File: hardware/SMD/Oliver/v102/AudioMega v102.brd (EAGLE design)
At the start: 77.1 x 44.9 mm, 74 parts, among them Q1 BC846ASMD, Q2 BC846ASMD, Q3 BC846ASMD, Q4 2N7002, Q5 BC846ASMD, U1 REG1117-5, U2 REG1117-3.3, U3 ATMEGA328-AU, U4 LM386M, X1 12MHz

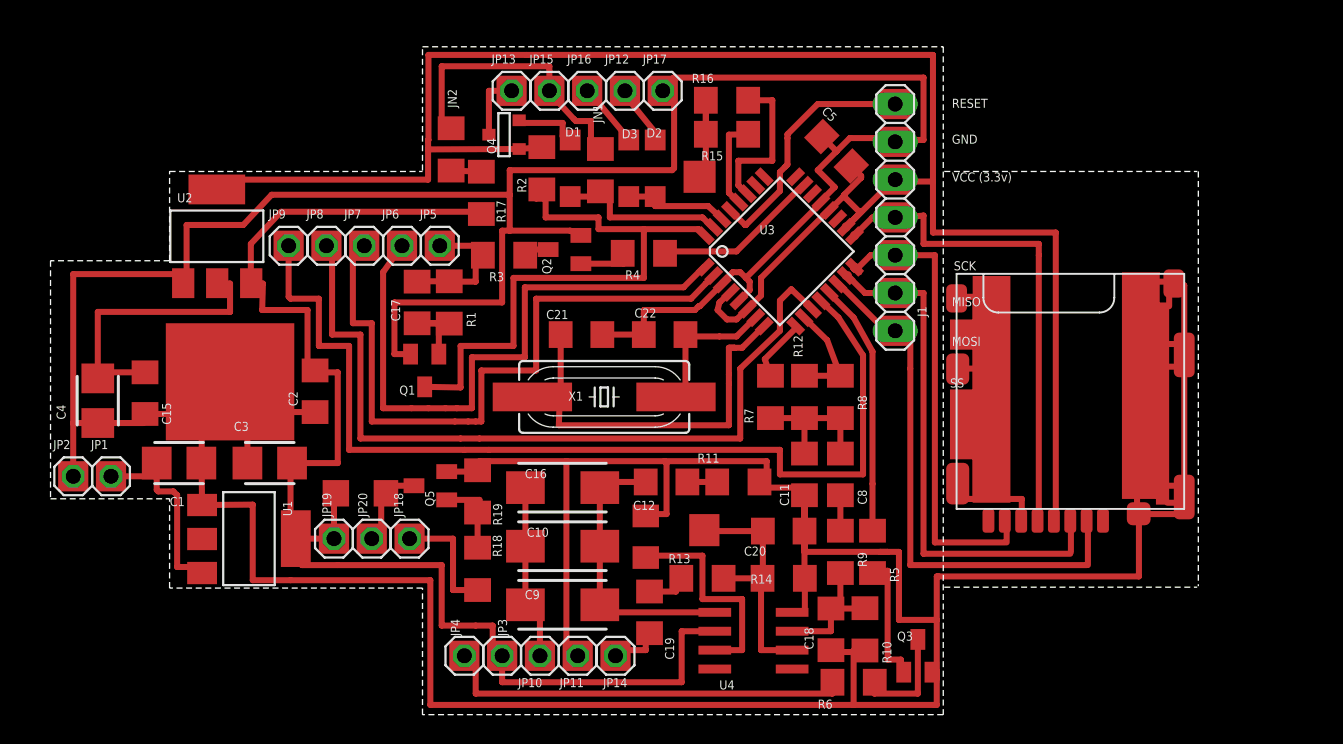
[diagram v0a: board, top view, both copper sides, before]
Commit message: updated v102 board + added connector for haptic motor + added last schematic changes from MikeB (connection to M64) + added last audio filter changes (filtering PWM noise) from Mike and Hans
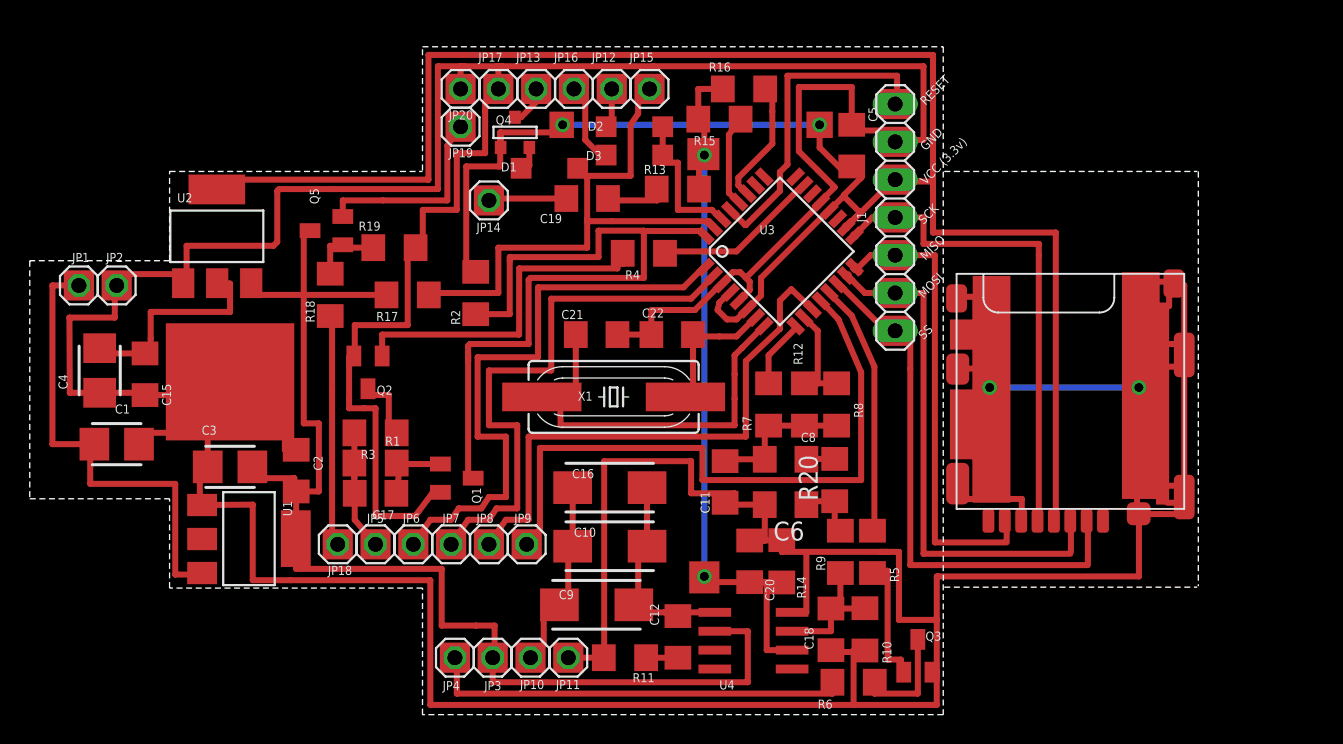
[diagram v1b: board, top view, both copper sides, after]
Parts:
- removed JN1, JN2: 0, resistor:R1206
- added C6: 330pf, resistor:C1206
- added R20: 47k, resistor:R1206
- R9: value 33k -> 47k
- moved JP14 31.8 mm to (29.5, 51.1)
- moved JP20 30.8 mm to (27.6, 58.5)
- moved JP19 29.0 mm to (27.6, 56.0)
- moved C19 28.1 mm to (36.1, 51.2), turned to 0 degrees
- moved R13 26.2 mm to (42.2, 51.8)
- moved JP9 25.7 mm to (32.0, 27.9)
- moved JP8 22.8 mm to (29.5, 27.9)
- moved R18 20.9 mm to (18.8, 44.7)
- moved JP7 20.9 mm to (26.9, 27.9)
- moved JP5 20.5 mm to (21.8, 27.9)
- moved JP6 20.1 mm to (24.4, 27.9)
- moved Q5 18.5 mm to (18.5, 49.0)
- moved R19 17.3 mm to (23.1, 47.9), turned to 0 degrees
- moved Q2 15.6 mm to (21.3, 39.5), turned to 180 degrees
- moved R3 14.7 mm to (21.8, 35.4)
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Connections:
- removed net N$14: U4.7
- removed net N$22: JN2.1, R17.1
- removed net N$44: JP20.1, Q5.3
- new net N$61: C8.1, R20.2
- net +5V: now also Q5.3; no longer JP19.1
- net GND: now also C6.2, JP20.1; no longer Q5.2
- net N$2: now also JP19.1, Q5.2; no longer JN1.2, JN2.2, JP15.1
- net N$24: now also C6.1, R20.1; no longer C8.1
- net N$38: now also JP15.1, R17.1; no longer JN1.1
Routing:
- net N$38: track 11.3 -> 41.1 mm
- net VOL_B: track 25.1 -> 54.2 mm, vias 0 -> 2
- net N$58: track 151.6 -> 178.3 mm, vias 0 -> 2
- net GND: track 362.3 -> 388.8 mm
- net N$30: track 66.6 -> 43.4 mm
- net N$9: track 3.58 -> 23.1 mm
- net N$32: track 14.8 -> 31.9 mm
- net N$31: track 53.9 -> 36.9 mm
- net CLK: track 39.7 -> 50.3 mm
- net N$40: track 8.03 -> 16.4 mm
- net N$35: track 45.3 -> 37.5 mm
- net N$44: track 6.94 -> 0.00 mm
- net +5V: track 93.6 -> 87.0 mm
- net N$2: track 19.6 -> 13.3 mm
- net N$6: track 17.5 -> 22.8 mm
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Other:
- board size 77.1 x 44.9 mm -> 78.5 x 44.9 mm

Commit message: updated v102 board - corrected BAT & GND pads
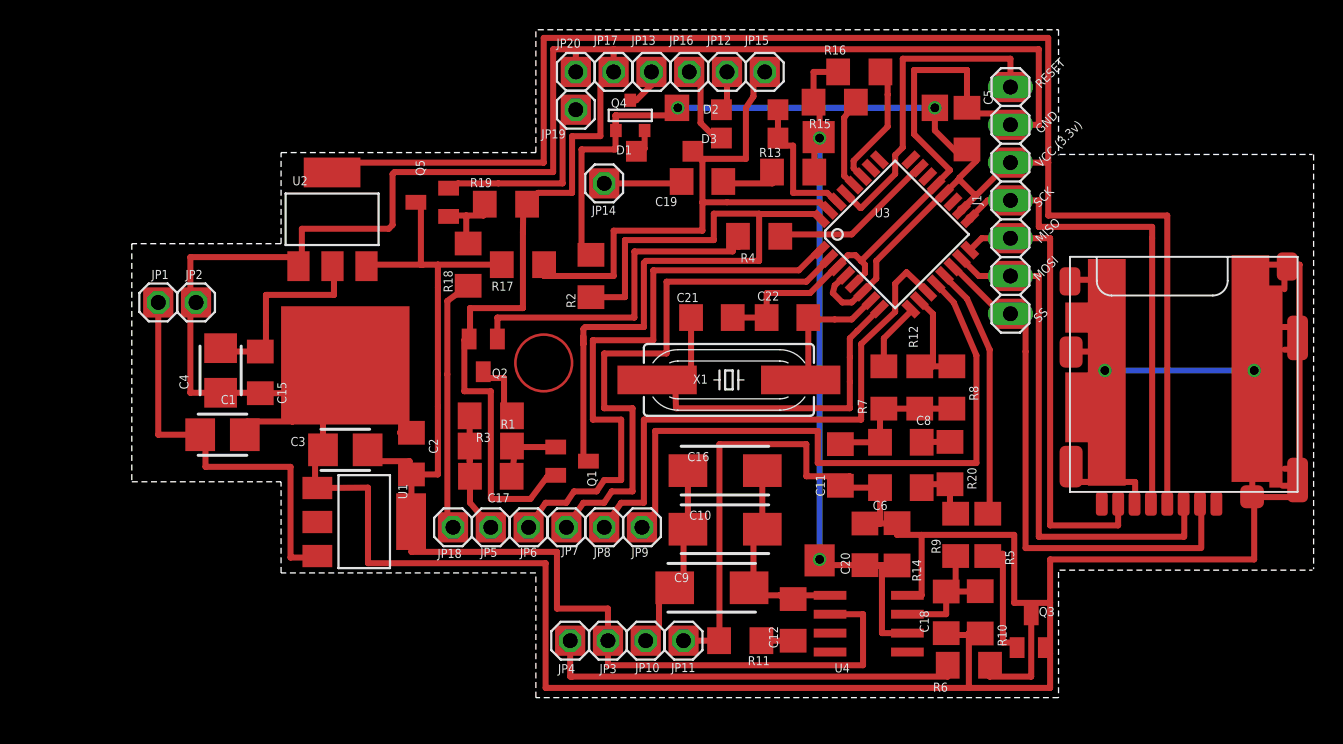
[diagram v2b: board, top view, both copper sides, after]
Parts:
- moved R18 9.49 mm to (28.1, 46.7)
- moved C4 8.13 mm to (11.4, 39.6)
- moved R19 8.04 mm to (30.6, 50.8)
- moved R17 8.01 mm to (31.8, 46.7)
- moved J1 7.83 mm to (64.5, 51.1)
- moved X1 7.83 mm to (45.6, 39.0)
- moved JP3 7.83 mm to (37.5, 21.5)
- moved R2 7.83 mm to (36.3, 46.0)
- moved C3 7.83 mm to (19.8, 34.3)
- moved C10 7.83 mm to (45.3, 29.0)
- moved C11 7.83 mm to (53.1, 33.3)
- moved C12 7.83 mm to (49.9, 22.9)
- moved C16 7.83 mm to (45.3, 32.9)
- moved C17 7.83 mm to (29.6, 32.5)
- moved C18 7.83 mm to (60.2, 23.4)
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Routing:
- net GND: track 388.8 -> 375.6 mm
- net N$32: track 31.9 -> 28.7 mm
- net N$46: track 0.76 -> 2.29 mm
- net N$58: track 178.3 -> 177.1 mm
- net N$6: track 22.8 -> 21.8 mm
- net N$4: track 30.5 -> 29.6 mm
- net VOL_B: track 54.2 -> 53.4 mm
- net N$40: track 16.4 -> 17.1 mm
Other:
- board size 78.5 x 44.9 mm -> 79.4 x 44.9 mm

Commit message: updated v102 board - checked for Gerber export - add Gerber files
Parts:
- moved C2 12.7 mm to (24.1, 46.7), turned to 270 degrees
- moved R15 0.25 mm to (52.7, 57.4)
- moved C1 0.13 mm to (11.6, 35.4)
- moved R20 0.13 mm to (60.6, 33.4)
- moved R19 0.13 mm to (30.6, 50.7)
- renumbered JP1 to UB+, JP10 to SP+, JP11 to SP-, JP12 to PD2, JP13 to TX, JP14 to BEP, JP15 to PD3, JP16 to RX, JP17 to GND, JP18 to PG2, JP19 to HAP+, JP2 to UGND, JP20 to HAPG, JP3 to BL+, JP4 to BL-, JP5 to PB7, JP6 to LCD0, JP7 to LCD1, JP8 to LCD2, JP9 to LCD3
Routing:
- net GND: track 375.6 -> 386.2 mm
- net +5V: track 87.1 -> 88.2 mm
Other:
- board text added: "(3.3v)"
- board text added: "RES"
- board text added: "TTL 5v uart"
- board text added: "VCC"
- board text added: "m64"
- board text removed: "RESET"
- board text removed: "VCC (3.3v)"

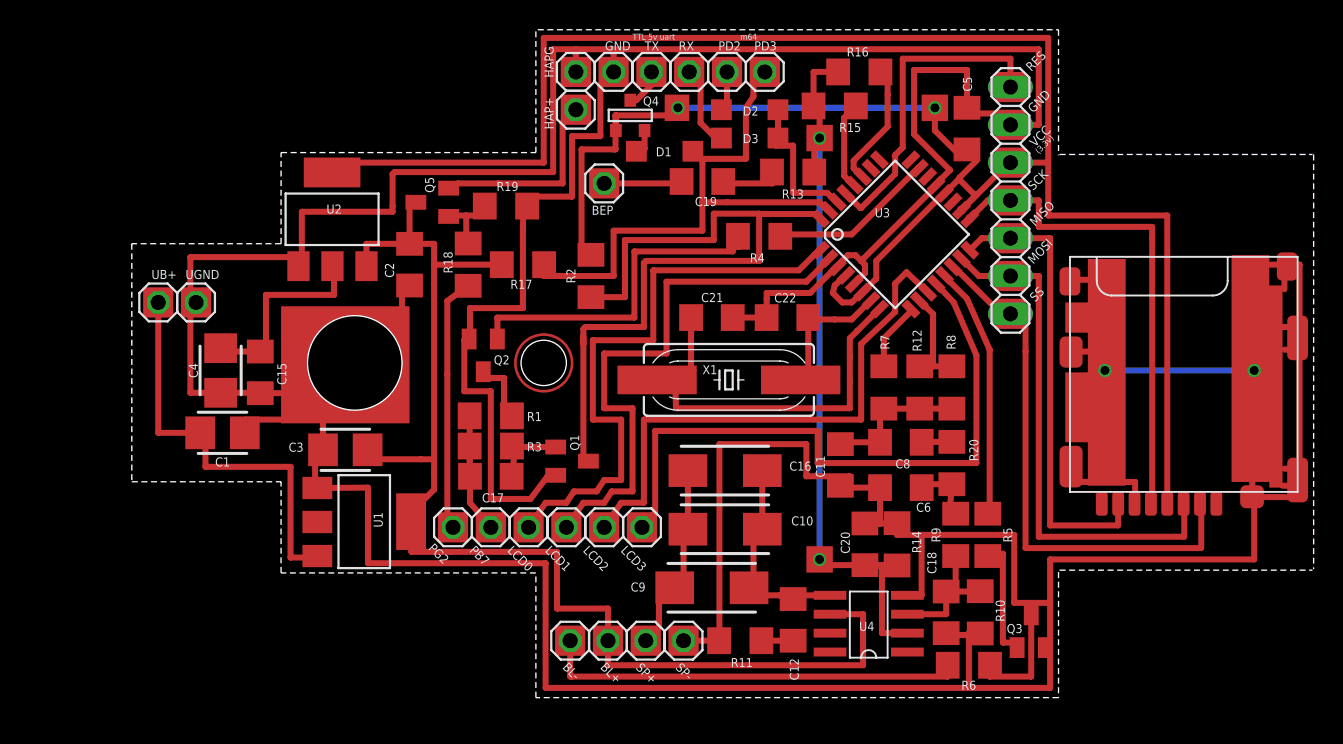
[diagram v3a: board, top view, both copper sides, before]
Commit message: updated v102 board - some minore changes for home etching
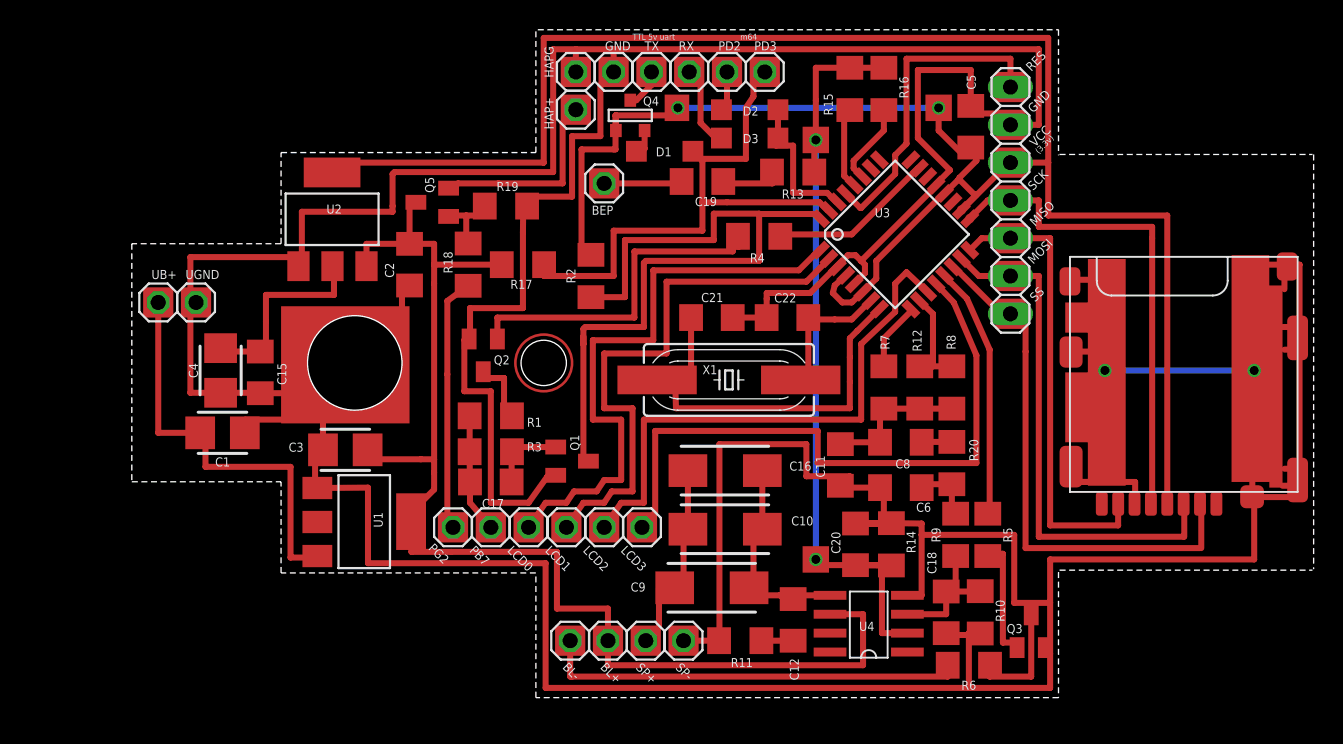
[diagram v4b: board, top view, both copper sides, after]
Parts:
- moved R16 2.01 mm to (56.0, 58.5), turned to 90 degrees
- moved R15 1.53 mm to (53.7, 58.5), turned to 90 degrees
- moved C20 0.64 mm to (54.1, 27.9)
- moved C17 0.38 mm to (29.6, 32.1)
- moved R1 0.38 mm to (29.6, 34.2)
- moved R14 0.38 mm to (56.5, 27.9)
- moved C5 0.28 mm to (61.8, 56.0)
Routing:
- net N$10: track 9.26 -> 5.59 mm
- net GND: track 386.2 -> 389.0 mm
- net VOL_B: track 53.8 -> 55.6 mm
- net N$13: track 6.18 -> 5.31 mm

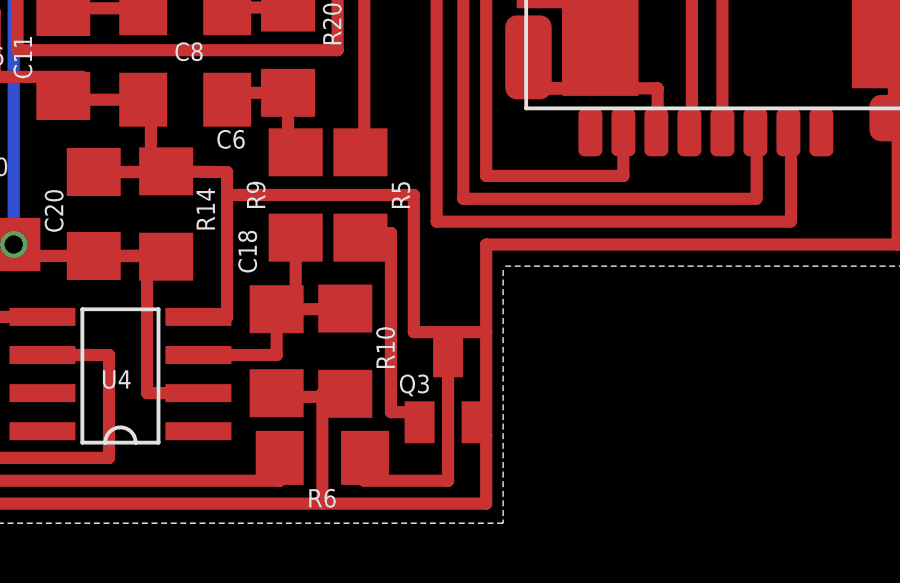
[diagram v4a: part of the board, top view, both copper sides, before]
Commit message: - fixed error near Q3
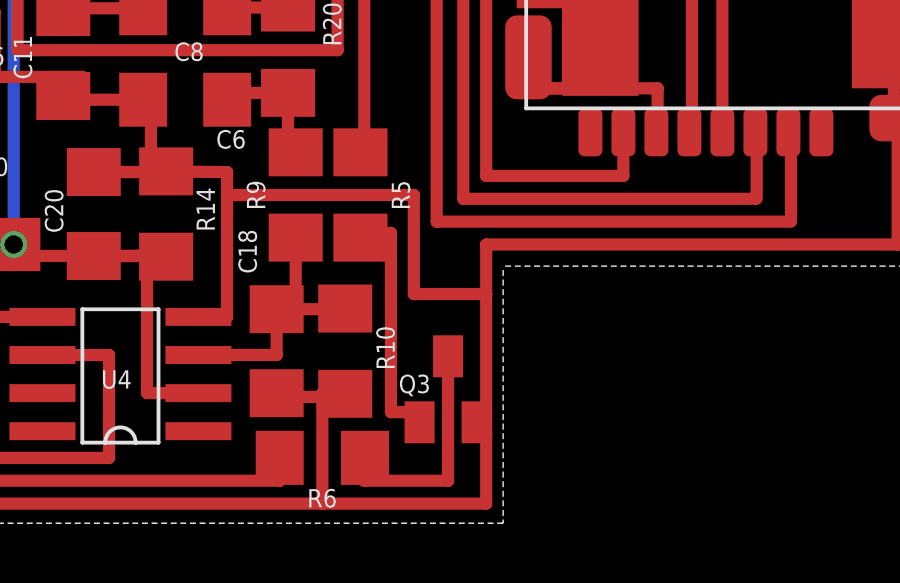
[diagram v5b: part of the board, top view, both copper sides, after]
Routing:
- net GND: track 389.0 -> 387.8 mm
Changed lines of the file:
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@@
 <layer number="17" name="Pads" color="2" fill="1" visible="yes" active="yes"/>
 <layer number="18" name="Vias" color="2" fill="1" visible="yes" active="yes"/>
-<layer number="19" name="Unrouted" color="13" fill="1" visible="yes" active="yes"/>
+<layer number="19" name="Unrouted" color="13" fill="1" visible="no" active="yes"/>
 <layer number="20" name="Dimension" color="15" fill="1" visible="yes" active="yes"/>
 <layer number="21" name="tPlace" color="7" fill="1" visible="yes" active="yes"/>
@@
 <layer number="42" name="bRestrict" color="1" fill="10" visible="no" active="yes"/>
 <layer number="43" name="vRestrict" color="2" fill="10" visible="no" active="yes"/>
-<layer number="44" name="Drills" color="7" fill="1" visible="yes" active="yes"/>
-<layer number="45" name="Holes" color="7" fill="1" visible="yes" active="yes"/>
+<layer number="44" name="Drills" color="7" fill="1" visible="no" active="yes"/>
+<layer number="45" name="Holes" color="7" fill="1" visible="no" active="yes"/>
 <layer number="46" name="Milling" color="3" fill="1" visible="no" active="yes"/>
 <layer number="47" name="Measures" color="7" fill="1" visible="yes" active="yes"/>
@@
 <wire x1="80.899" y1="31.115" x2="83.947" y2="31.115" width="0.4064" layer="1"/>
 <wire x1="83.947" y1="31.115" x2="83.947" y2="46.736" width="0.4064" layer="1"/>
-<wire x1="64.77" y1="28.575" x2="64.77" y2="24.003" width="0.4064" layer="1"/>
-<wire x1="64.77" y1="24.003" x2="67.183" y2="24.003" width="0.4064" layer="1"/>
-<wire x1="67.183" y1="26.924" x2="67.183" y2="24.003" width="0.4064" layer="1"/>
+<wire x1="64.77" y1="28.575" x2="64.77" y2="25.273" width="0.4064" layer="1"/>
+<wire x1="64.77" y1="25.273" x2="67.183" y2="25.273" width="0.4064" layer="1"/>
+<wire x1="67.183" y1="26.924" x2="67.183" y2="25.273" width="0.4064" layer="1"/>
 <contactref element="C6" pad="2"/>
 <wire x1="61.722" y1="21.971" x2="62.459" y2="21.971" width="0.4064" layer="1"/>
@@
 <wire x1="9.398" y1="44.196" x2="9.398" y2="38.124" width="0.4064" layer="1"/>
 <wire x1="9.779" y1="44.196" x2="9.398" y2="44.196" width="0.4064" layer="1"/>
-<wire x1="67.183" y1="20.574" x2="67.183" y2="24.003" width="0.4064" layer="1"/>
+<wire x1="67.183" y1="20.574" x2="67.183" y2="25.273" width="0.4064" layer="1"/>
 <wire x1="66.99" y1="20.574" x2="67.183" y2="20.574" width="0.4064" layer="1"/>
 <wire x1="66.421" y1="56.134" x2="64.516" y2="56.134" width="0.4064" layer="1"/>
